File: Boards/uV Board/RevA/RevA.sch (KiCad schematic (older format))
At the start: 2 parts

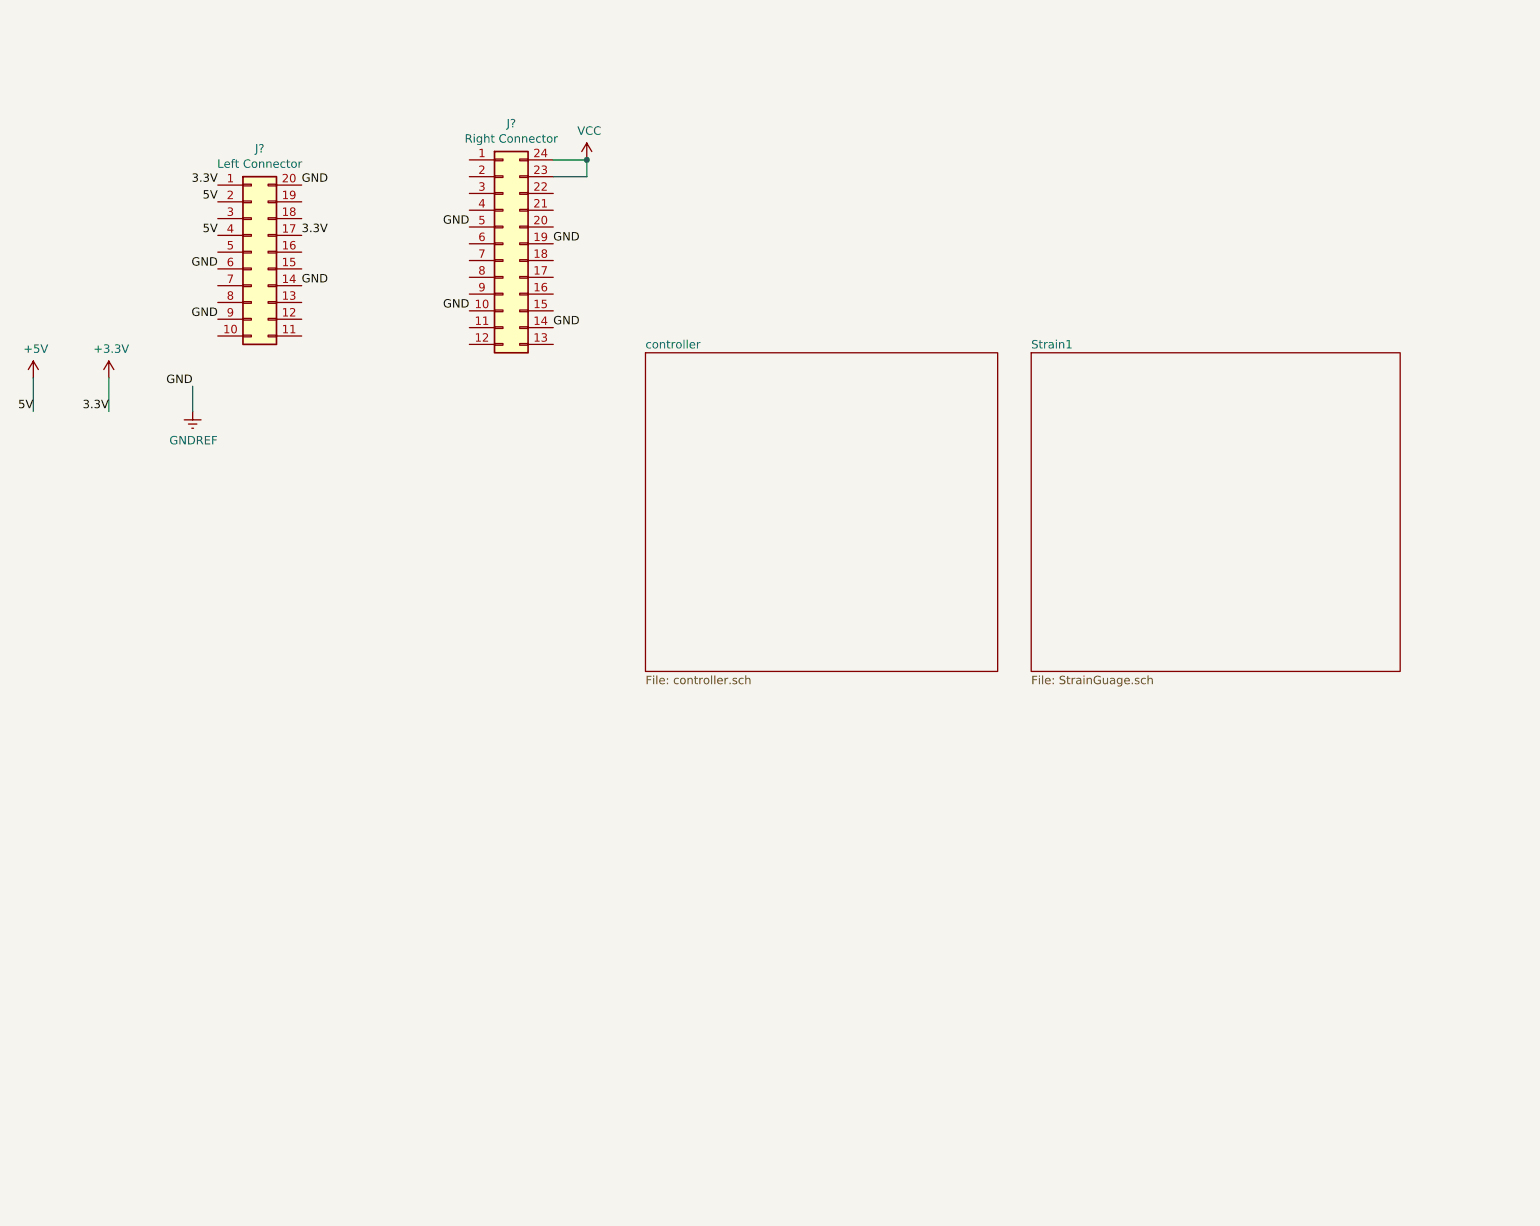
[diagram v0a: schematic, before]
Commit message: Added thermocouple sheet
Also moved around some stuff for clarity, and added some text.
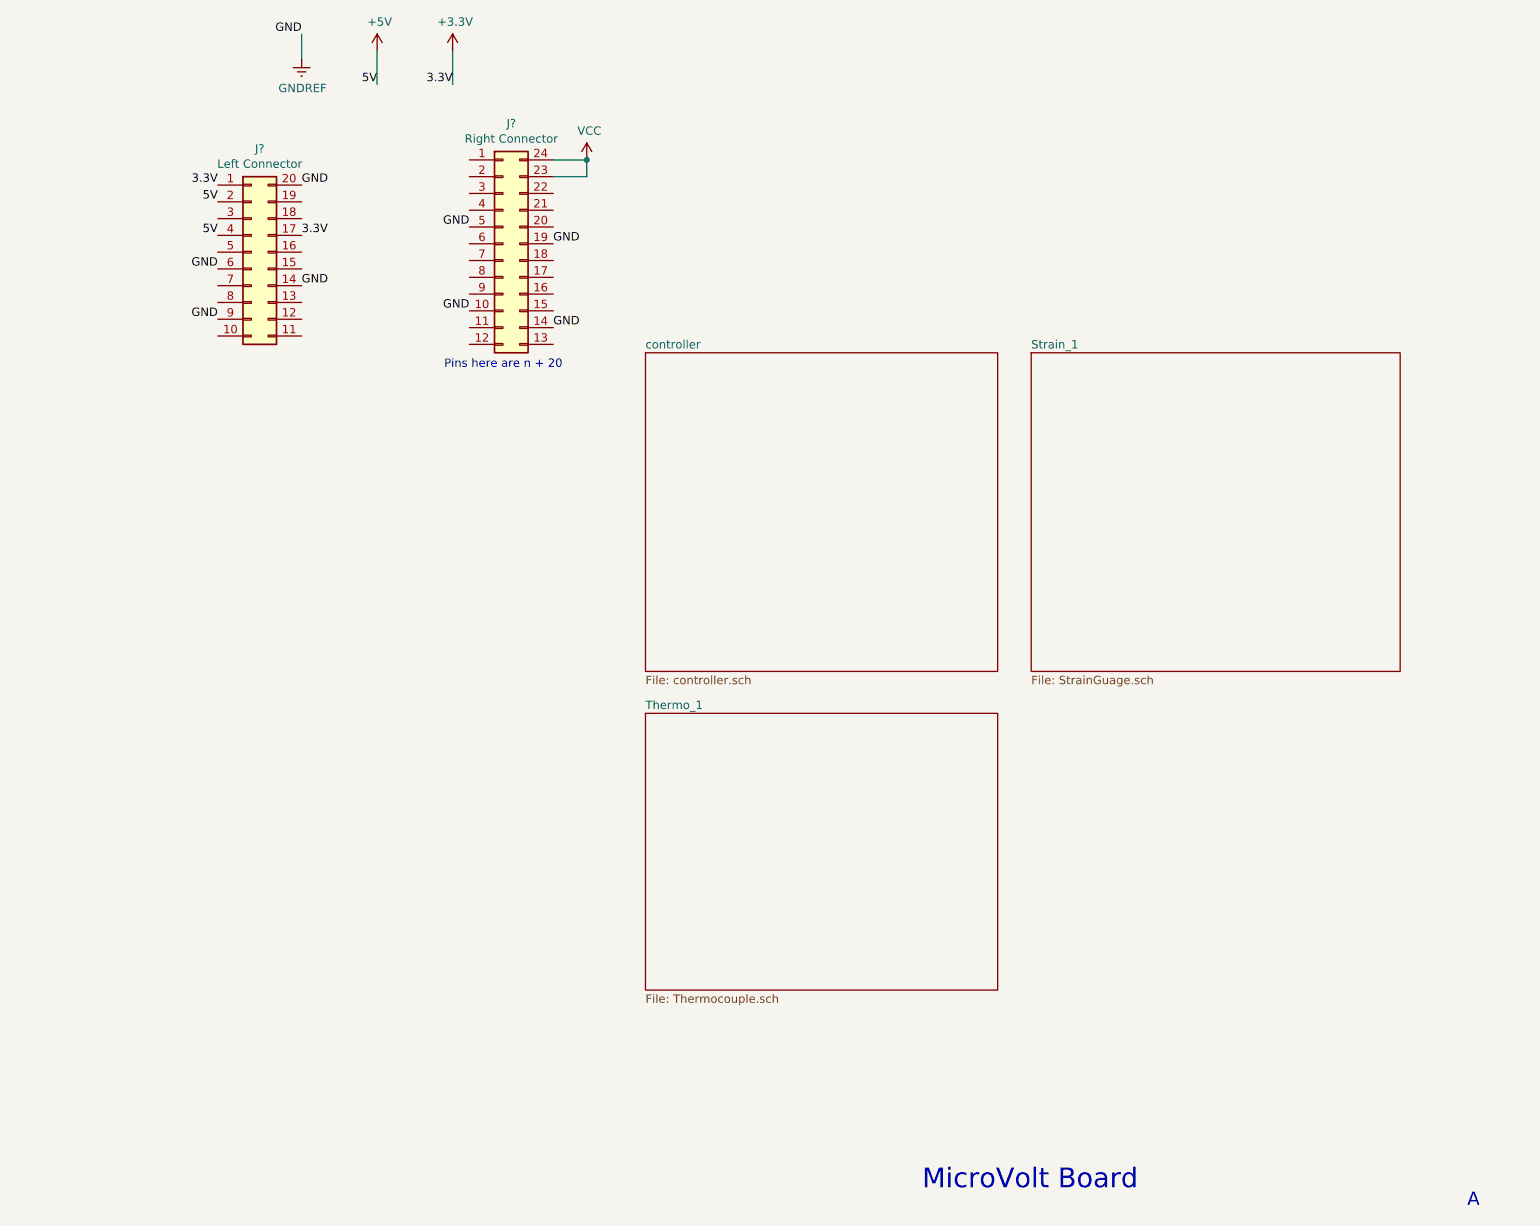
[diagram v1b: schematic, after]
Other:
- note added: "A"
- note added: "MicroVolt Board"
- note added: "Pins here are n + 20\n"
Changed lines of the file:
@@
 $Descr A4 11693 8268
 encoding utf-8
-Sheet 1 3
+Sheet 1 4
 Title ""
 Date ""
@@
 L power:GNDREF #PWR?
 U 1 1 614F8C33
-P 3000 2900
-F 0 "#PWR?" H 3000 2650 50  0001 C CNN
-F 1 "GNDREF" H 3005 2727 50  0000 C CNN
-F 2 "" H 3000 2900 50  0001 C CNN
-F 3 "" H 3000 2900 50  0001 C CNN
-	1    3000 2900
+P 3650 800
+F 0 "#PWR?" H 3650 550 50  0001 C CNN
+F 1 "GNDREF" H 3655 627 50  0000 C CNN
+F 2 "" H 3650 800 50  0001 C CNN
+F 3 "" H 3650 800 50  0001 C CNN
+	1    3650 800
 	1    0    0    -1
 $EndComp
-Text Label 3000 2750 2    50   ~ 0
+Text Label 3650 650  2    50   ~ 0
 GND
 Wire Wire Line
-	3000 2750 3000 2900
+	3650 650  3650 800
 $Comp
 L power:+3.3V #PWR?
 U 1 1 614FB62C
-P 2500 2700
-F 0 "#PWR?" H 2500 2550 50  0001 C CNN
-F 1 "+3.3V" H 2515 2873 50  0000 C CNN
-F 2 "" H 2500 2700 50  0001 C CNN
-F 3 "" H 2500 2700 50  0001 C CNN
-	1    2500 2700
+P 4550 750
+F 0 "#PWR?" H 4550 600 50  0001 C CNN
+F 1 "+3.3V" H 4565 923 50  0000 C CNN
+F 2 "" H 4550 750 50  0001 C CNN
+F 3 "" H 4550 750 50  0001 C CNN
+	1    4550 750
 	1    0    0    -1
 $EndComp
-Text Label 2500 2900 2    50   ~ 0
+Text Label 4550 950  2    50   ~ 0
 3.3V
 Wire Wire Line
-	2500 2900 2500 2700
+	4550 950  4550 750
 $Comp
 L power:+5V #PWR?
 U 1 1 614FCDE4
-P 2050 2700
-F 0 "#PWR?" H 2050 2550 50  0001 C CNN
-F 1 "+5V" H 2065 2873 50  0000 C CNN
-F 2 "" H 2050 2700 50  0001 C CNN
-F 3 "" H 2050 2700 50  0001 C CNN
-	1    2050 2700
+P 4100 750
+F 0 "#PWR?" H 4100 600 50  0001 C CNN
+F 1 "+5V" H 4115 923 50  0000 C CNN
+F 2 "" H 4100 750 50  0001 C CNN
+F 3 "" H 4100 750 50  0001 C CNN
+	1    4100 750
 	1    0    0    -1
 $EndComp
-Text Label 2050 2900 2    50   ~ 0
+Text Label 4100 950  2    50   ~ 0
 5V
 Wire Wire Line
-	2050 2900 2050 2700
+	4100 950  4100 750
 $Sheet
 S 5700 2550 2100 1900
@@
 S 8000 2550 2200 1900
 U 614FDE40
-F0 "Strain1" 50
+F0 "Strain_1" 50
 F1 "StrainGuage.sch" 50
 $EndSheet
+$Sheet
+S 5700 4700 2100 1650
+U 614DF1EE
+F0 "Thermo_1" 50
+F1 "Thermocouple.sch" 50
+$EndSheet
+Text Notes 4500 2650 0    50   ~ 0
+Pins here are n + 20\n
+Text Notes 10600 7650 0    79   ~ 0
+A
+Text Notes 7350 7550 0    118  ~ 0
+MicroVolt Board
 $EndSCHEMATC

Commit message: Added a lot to the microVolt board.
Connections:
- net Reset: now reaches J?.22 (Pin_22)
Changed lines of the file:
@@
 $Descr A4 11693 8268
 encoding utf-8
-Sheet 1 4
+Sheet 1 6
 Title ""
 Date ""
@@
 	4100 950  4100 750
 $Sheet
-S 5700 2550 2100 1900
+S 5750 2550 2100 1900
 U 614FD8C2
 F0 "controller" 50
 F1 "controller.sch" 50
-$EndSheet
-$Sheet
-S 8000 2550 2200 1900
+F2 "GND" I R 7850 2800 50
+F3 "5V" I R 7850 2650 50
+F4 "Reset" I L 5750 3000 50
+F5 "CAN_H" I L 5750 3500 50
+F6 "CAN_L" I L 5750 3650 50
+F7 "Strain_4" I R 7850 3600 50
+F8 "Strain_3" I R 7850 3750 50
+F9 "Strain_2" I R 7850 3900 50
+F10 "Strain_1" I R 7850 4050 50
+$EndSheet
+$Sheet
+S 8500 2550 800  700
 U 614FDE40
 F0 "Strain_1" 50
 F1 "StrainGuage.sch" 50
-$EndSheet
-$Sheet
-S 5700 4700 2100 1650
-U 614DF1EE
-F0 "Thermo_1" 50
-F1 "Thermocouple.sch" 50
+F2 "5V" I L 8500 2700 50
+F3 "GND" I L 8500 2800 50
+F4 "Strain_Out" I L 8500 2900 50
 $EndSheet
 Text Notes 4500 2650 0    50   ~ 0
@@
 Text Notes 7350 7550 0    118  ~ 0
 MicroVolt Board
+$Sheet
+S 9450 2550 800  700
+U 6153C564
+F0 "Strain_2" 50
+F1 "StrainGuage.sch" 50
+F2 "5V" I R 10250 2700 50
+F3 "GND" I R 10250 2800 50
+F4 "Strain_Out" I R 10250 2900 50
+$EndSheet
+$Sheet
+S 8500 3550 800  700
+U 61575900
+F0 "Strain_3" 50
+F1 "StrainGuage.sch" 50
+F2 "5V" I L 8500 3700 50
+F3 "GND" I L 8500 3800 50
+F4 "Strain_Out" I L 8500 3900 50
+$EndSheet
+$Sheet
+S 9450 3550 800  700
+U 61575905
+F0 "Strain_4" 50
+F1 "StrainGuage.sch" 50
+F2 "5V" I R 10250 3700 50
+F3 "GND" I R 10250 3800 50
+F4 "Strain_Out" I R 10250 3900 50
+$EndSheet
+Wire Wire Line
+	8500 3700 8350 3700
+Wire Wire Line
+	8350 3700 8350 2700
+Wire Wire Line
+	8350 2700 8500 2700
+Wire Wire Line
+	10250 2700 10400 2700
+Wire Wire Line
+	10400 2700 10400 3700
+Wire Wire Line
+	10400 3700 10250 3700
+Text Label 8850 2000 0    50   ~ 0
+5V
+Text Label 9150 2000 0    50   ~ 0
+GND
+Wire Wire Line
+	8350 2700 8350 2200
+Wire Wire Line
+	8350 2200 8850 2200
+Connection ~ 8350 2700
+Wire Wire Line
+	10400 2700 10400 2200
+Wire Wire Line
+	10400 2200 8850 2200
+Wire Wire Line
+	8850 2200 8850 2000
+Connection ~ 10400 2700
+Wire Wire Line
+	8500 2800 8450 2800
+Wire Wire Line
+	8450 2800 8450 2300
+Wire Wire Line
+	8450 2300 9150 2300
+Wire Wire Line
+	9150 2300 9150 2000
+Wire Wire Line
+	8500 3800 8450 3800
+Wire Wire Line
+	8450 3800 8450 2800
+Connection ~ 8450 2800
+Wire Wire Line
+	10250 3800 10300 3800
+Wire Wire Line
+	10300 3800 10300 2800
+Wire Wire Line
+	10300 2800 10250 2800
+Wire Wire Line
+	10300 2800 10300 2300
+Wire Wire Line
+	10300 2300 9150 2300
+Connection ~ 10300 2800
+Connection ~ 9150 2300
+Connection ~ 8850 2200
+Wire Wire Line
+	8350 2200 8000 2200
+Wire Wire Line
+	8000 2200 8000 2650
+Wire Wire Line
+	8000 2650 7850 2650
+Connection ~ 8350 2200
+Wire Wire Line
+	8450 2300 8150 2300
+Wire Wire Line
+	8150 2300 8150 2800
+Wire Wire Line
+	8150 2800 7850 2800
+Connection ~ 8450 2300
+Wire Wire Line
+	8500 2900 8200 2900
+Text Label 7850 3900 0    50   ~ 0
+Strain_2
+Text Label 7850 3600 0    50   ~ 0
+Strain_4
+Text Label 10600 2900 0    50   ~ 0
+Strain2
+Text Label 10600 3900 0    50   ~ 0
+Stain_4
+Wire Wire Line
+	10250 2900 10600 2900
+Wire Wire Line
+	10250 3900 10600 3900
+Wire Wire Line
+	8200 2900 8200 4050
+Wire Wire Line
+	7850 4050 8200 4050
+Wire Wire Line
+	7850 3750 8050 3750
+Wire Wire Line
+	8050 3750 8050 3900
+Wire Wire Line
+	8050 3900 8500 3900
+Text Label 5150 1600 0    50   ~ 0
+Reset
+Text Label 5750 3000 2    50   ~ 0
+Reset
 $EndSCHEMATC
